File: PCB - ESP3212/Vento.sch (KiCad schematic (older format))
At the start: 0 parts

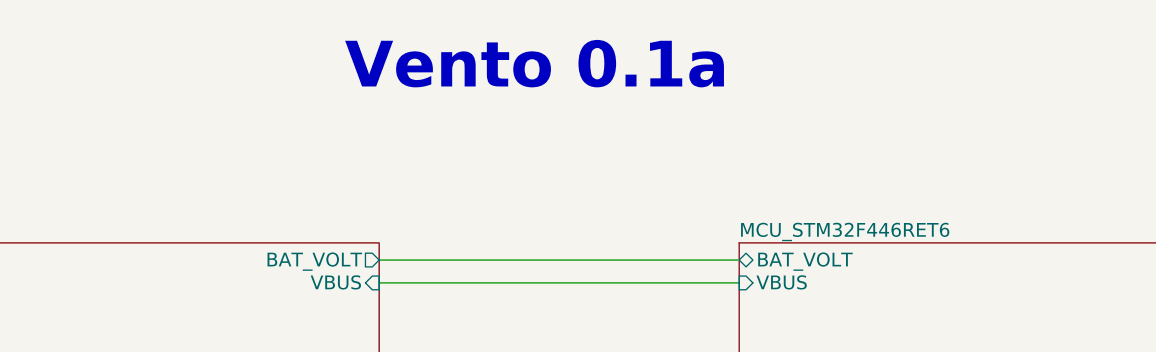
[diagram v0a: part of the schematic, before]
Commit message: On/Off And Cleanup
Onoff Switch added, PCB extended 1mm to accomodated everything. routing
and traes cleaned up. Heat sinking ground pours added to the BQ chip
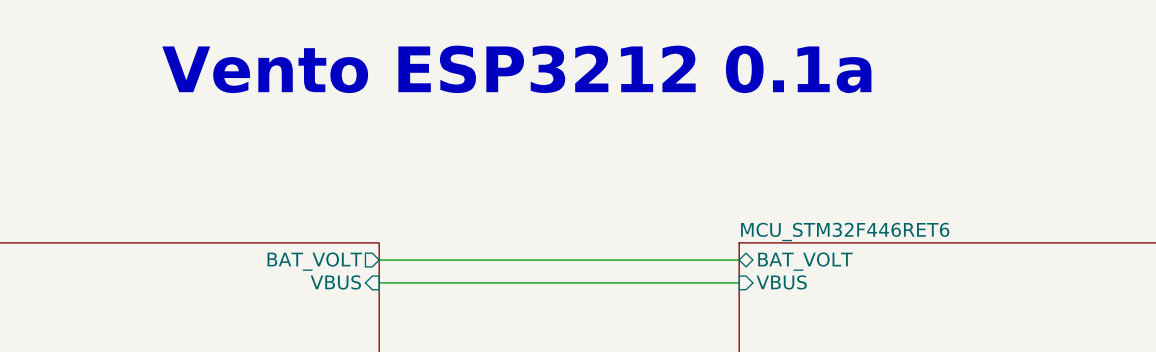
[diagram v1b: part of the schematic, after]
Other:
- note added: "Vento ESP3212 0.1a"
- note removed: "Vento 0.1a"
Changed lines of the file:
@@
 F8 "ESP_ST_RST" I R 5700 4425 60
 $EndSheet
-Text Notes 5275 1250 0    200  ~ 40
-Vento 0.1a
+Text Notes 4475 1275 0    200  ~ 40
+Vento ESP3212 0.1a
 Wire Wire Line
 	5425 1975 7000 1975
